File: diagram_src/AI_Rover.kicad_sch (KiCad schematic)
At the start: 11 parts, among them J1 GPIO_PINS, J2 LOGIC_PINS, J3 LOGIC_PINS, J5 POWER_PINS, J6 POWER_PINS, M1 MOTOR_DC_LEFT, M2 MOTOR_DC_RIGHT, SW1 MAIN_POWER_SWITCH

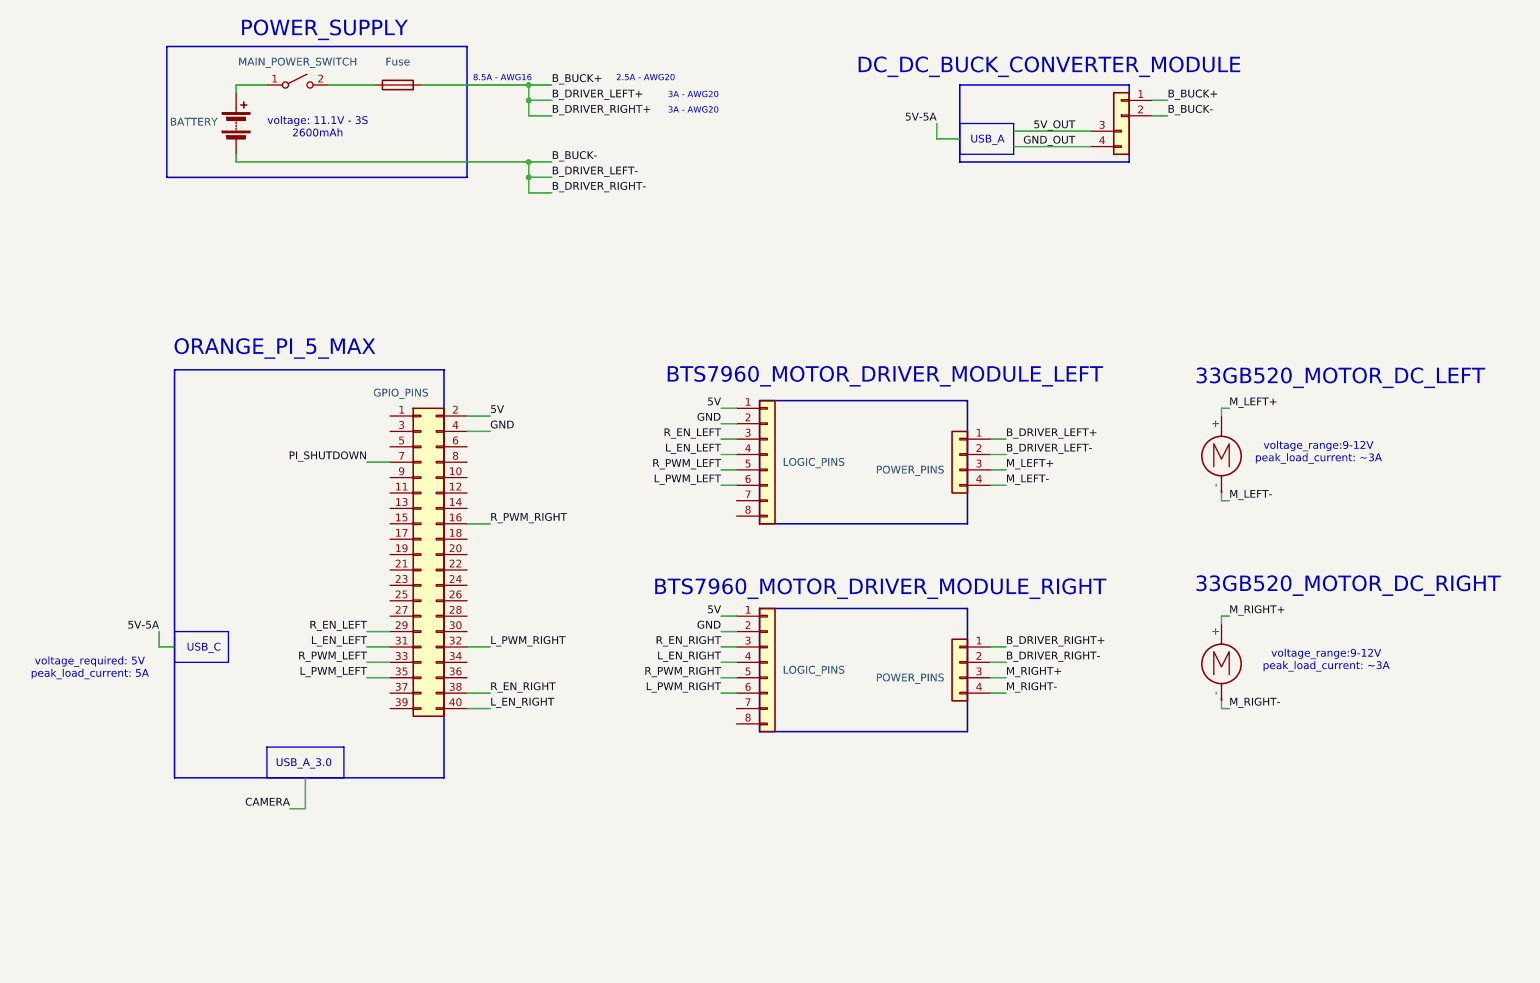
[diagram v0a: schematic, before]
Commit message: Hardware: Add IMU and small improvements to Wiring Schematic
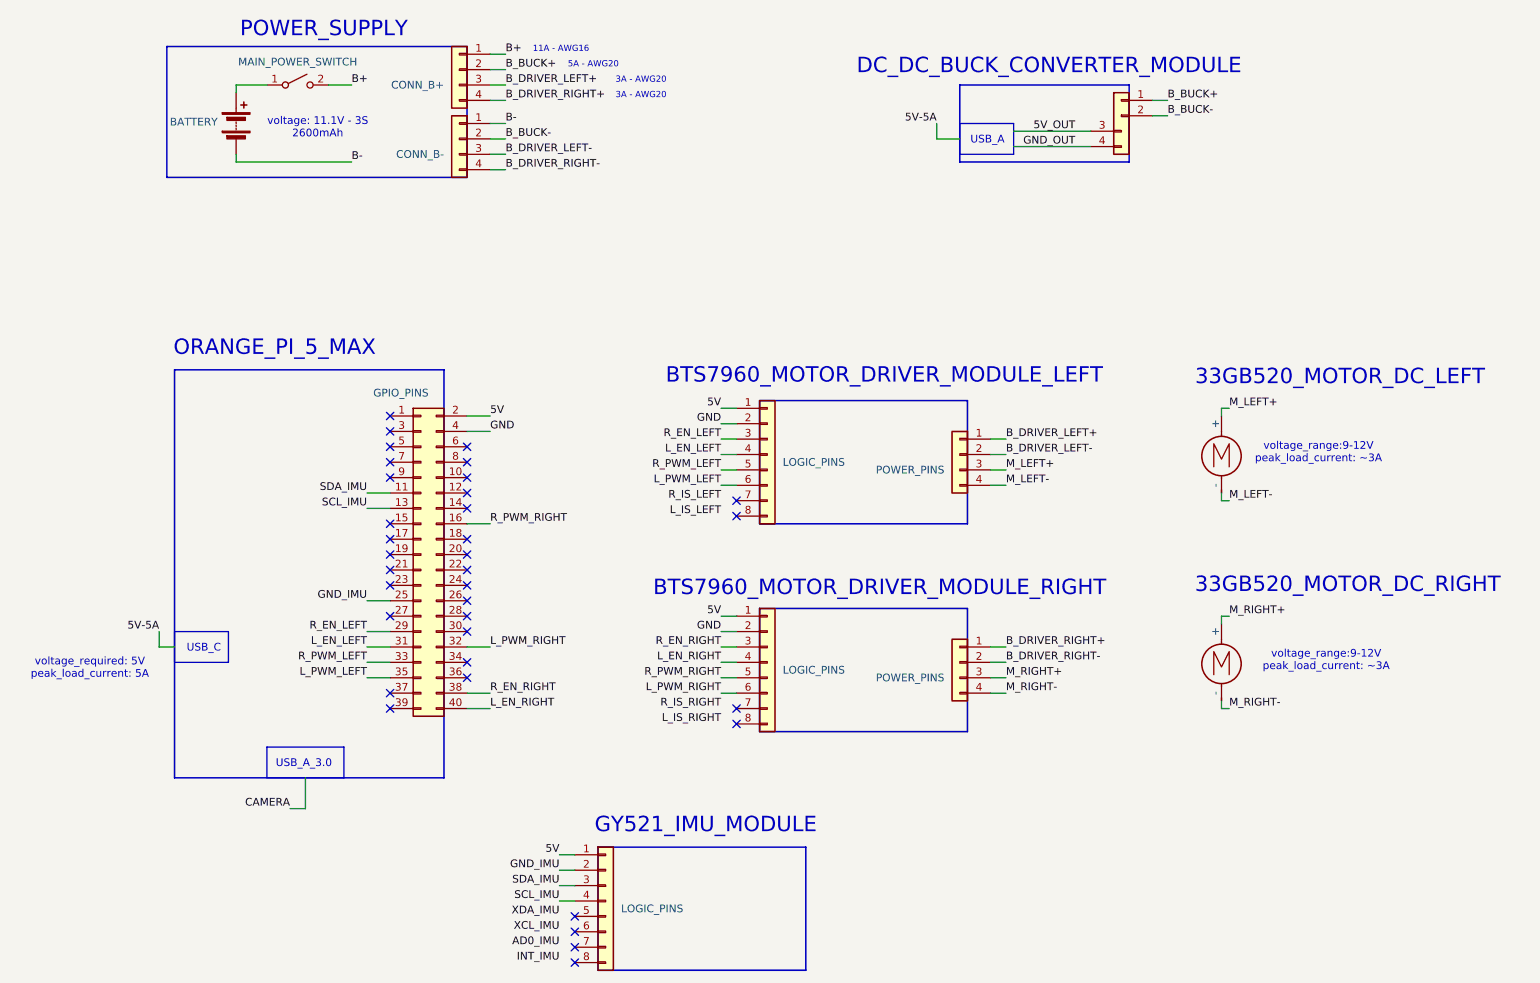
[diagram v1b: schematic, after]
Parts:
- removed F1: Fuse, symbol Device:Fuse
- added J?: CONN_B+, symbol Connector_Generic:Conn_01x04
- added J?: LOGIC_PINS, symbol Connector_Generic:Conn_01x08
- added J?: CONN_B-, symbol Connector_Generic:Conn_01x04
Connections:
- net 5V: now also J?.1 (Pin_1)
- net B_BUCK+: now also J?.2 (Pin_2); no longer J5.1 (Pin_1), J6.1 (Pin_1)
- net B_BUCK-: now also J?.2 (Pin_2); no longer BT1.2 (-), J5.2 (Pin_2), J6.2 (Pin_2)
- net SDA_IMU: now reaches J1.11 (Pin_11)
- net SDA_IMU: now also J?.3 (Pin_3)
- net SCL_IMU: now reaches J1.13 (Pin_13)
- net SCL_IMU: now also J?.4 (Pin_4)
- net GND_IMU: now reaches J1.25 (Pin_25)
- net GND_IMU: now also J?.2 (Pin_2)
- net B+: now reaches SW1.2 (B)
- net B+: now also J?.1 (Pin_1)
- net PI_SHUTDOWN: no longer names the net of J1.7 (Pin_7)
- new net B-: BT1.2 (-), J?.1 (Pin_1)
- new net B_DRIVER_LEFT+: J5.1 (Pin_1), J?.3 (Pin_3)
- new net B_DRIVER_LEFT-: J5.2 (Pin_2), J?.3 (Pin_3)
- new net B_DRIVER_RIGHT+: J6.1 (Pin_1), J?.4 (Pin_4)
- new net B_DRIVER_RIGHT-: J6.2 (Pin_2), J?.4 (Pin_4)
- no-connect marks 0 -> 35
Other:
- note added: "11A - AWG16"
- note added: "5A - AWG20"
- note added: "GY521_IMU_MODULE"
- note removed: "2.5A - AWG20"
- note removed: "8.5A - AWG16"

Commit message: Hardware: Fix wiring issue, cause of GPIO Pins misalignment of 5V pin
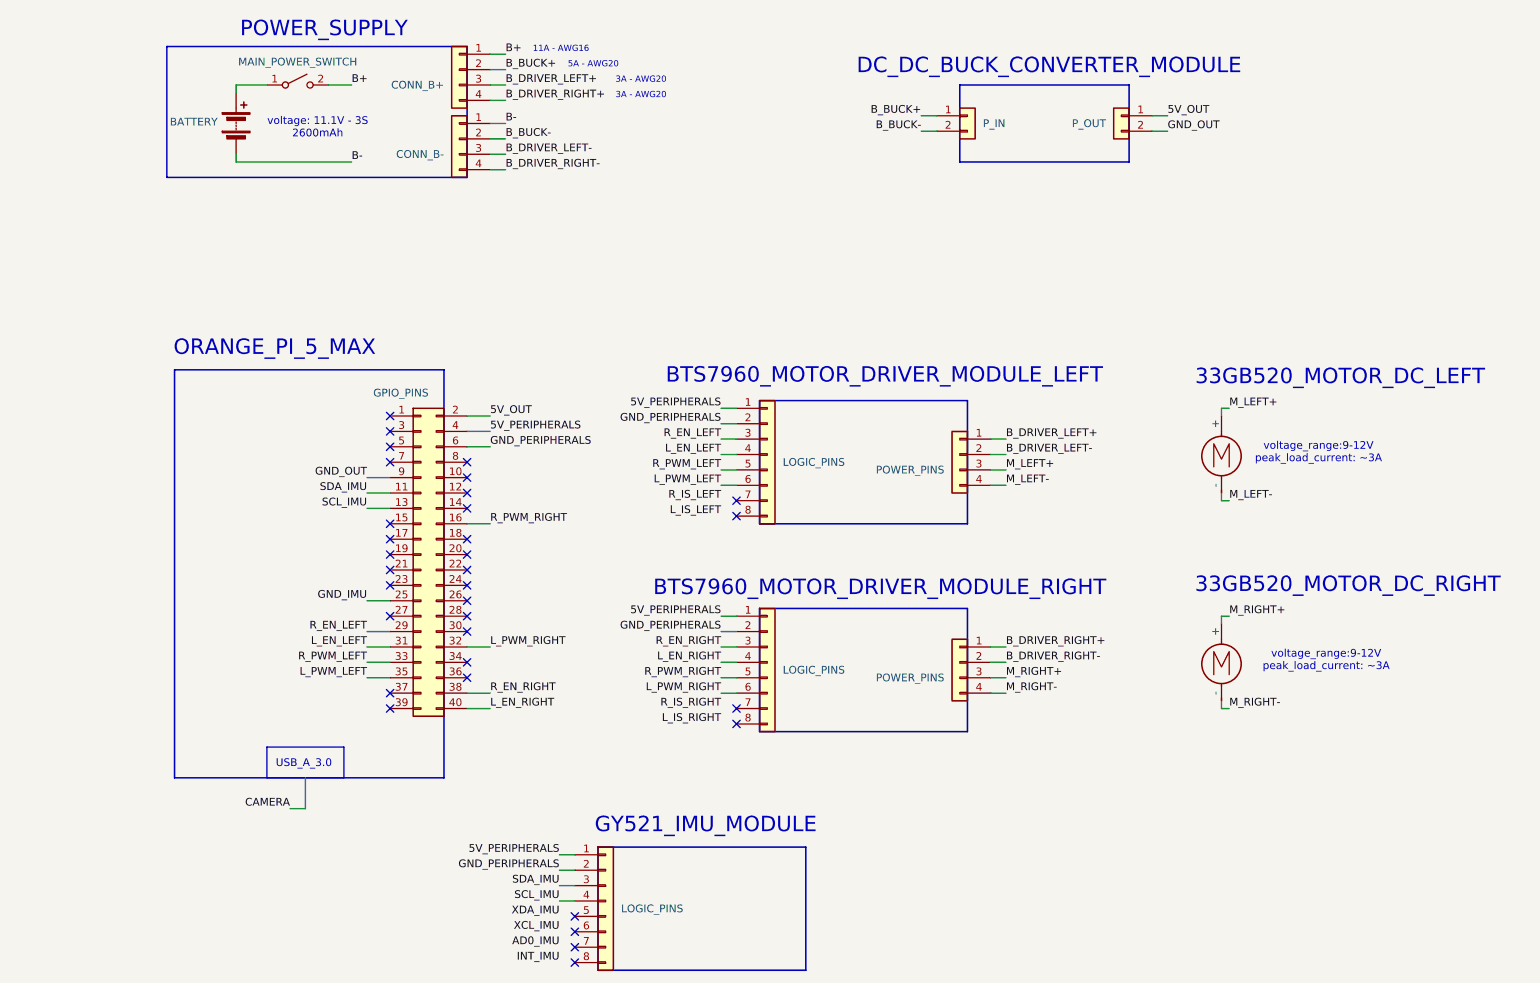
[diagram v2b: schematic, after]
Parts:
- removed J4: (no value), symbol Connector_Generic:Conn_01x04
- added J?: P_OUT, symbol Connector_Generic:Conn_01x02
- added J?: P_IN, symbol Connector_Generic:Conn_01x02
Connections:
- net 5V_OUT: now also J1.2 (Pin_2), J?.1 (Pin_1)
- net B_BUCK+: now also J?.1 (Pin_1)
- net B_BUCK-: now also J?.2 (Pin_2)
- net GND_IMU: no longer J?.2 (Pin_2)
- net GND_OUT: now also J1.9 (Pin_9), J?.2 (Pin_2)
- net GND_PERIPHERALS: now reaches J1.6 (Pin_6)
- net GND_PERIPHERALS: now also J2.2 (Pin_2), J3.2 (Pin_2), J?.2 (Pin_2)
- net 5V renamed 5V_PERIPHERALS
- net 5V_PERIPHERALS: now also J1.4 (Pin_4); no longer J1.2 (Pin_2)
- removed net GND: J1.4 (Pin_4), J2.2 (Pin_2), J3.2 (Pin_2)
- no-connect marks 35 -> 33
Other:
- note removed: "USB_A"
- note removed: "USB_C"
- note removed: "voltage_required: 5V peak_load_current: 5A"

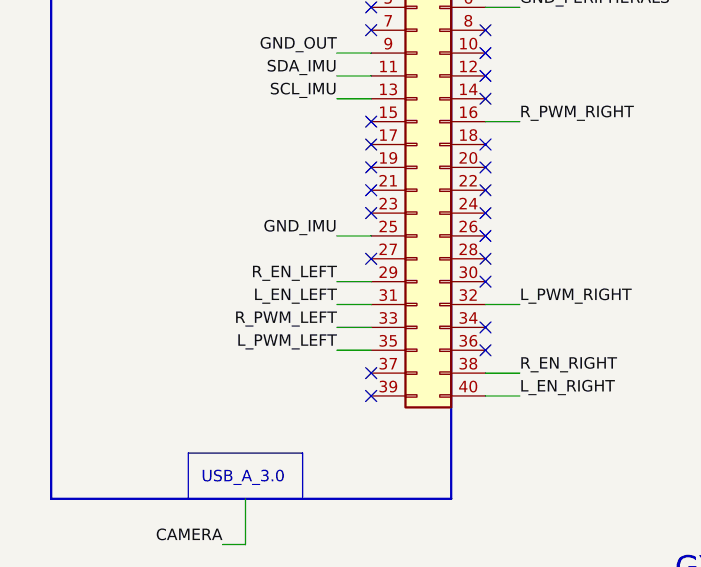
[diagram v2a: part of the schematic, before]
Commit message: Hardware: Fix PWM wiring issue of same PWM line where two different control signals are required
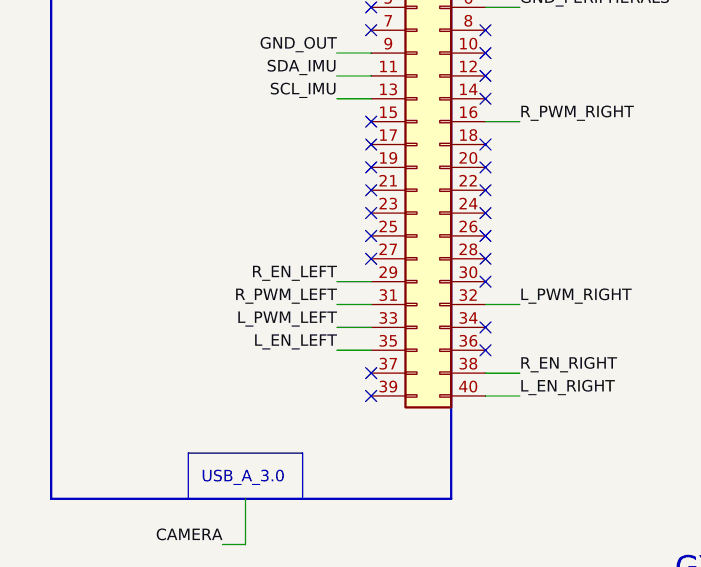
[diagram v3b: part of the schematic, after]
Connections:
- net L_EN_LEFT: now also J1.35 (Pin_35); no longer J1.31 (Pin_31)
- net L_PWM_LEFT: now also J1.33 (Pin_33); no longer J1.35 (Pin_35)
- net R_PWM_LEFT: now also J1.31 (Pin_31); no longer J1.33 (Pin_33)
- net GND_IMU: no longer names the net of J1.25 (Pin_25)
- no-connect marks 33 -> 34
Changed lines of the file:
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@@
+	)
+	(no_connect
+		(at 83.82 120.65)
 	)
 	(no_connect
@@
 	(wire
 		(pts
-			(xy 80.01 120.65) (xy 83.82 120.65)
-		)
-		(stroke
-			(width 0)
-			(type default)
-		)
-	)
-	(wire
-		(pts
 			(xy 222.25 104.14) (xy 220.98 104.14)
 		)
@@
 			(width 0)
 			(type default)
-		)
-	)
-	(label "GND_IMU"
-		(at 80.01 120.65 180)
-		(effects
-			(font
-				(size 1.27 1.27)
-			)
-			(justify right bottom)
 		)
 	)
@@
 		)
 	)
-	(label "R_PWM_LEFT"
+	(label "L_PWM_LEFT"
 		(at 80.01 130.81 180)
 		(effects
@@
 		)
 	)
-	(label "L_PWM_LEFT"
+	(label "L_EN_LEFT"
 		(at 80.01 133.35 180)
 		(effects
@@
 		)
 	)
-	(label "L_EN_LEFT"
+	(label "R_PWM_LEFT"
 		(at 80.01 128.27 180)
 		(effects

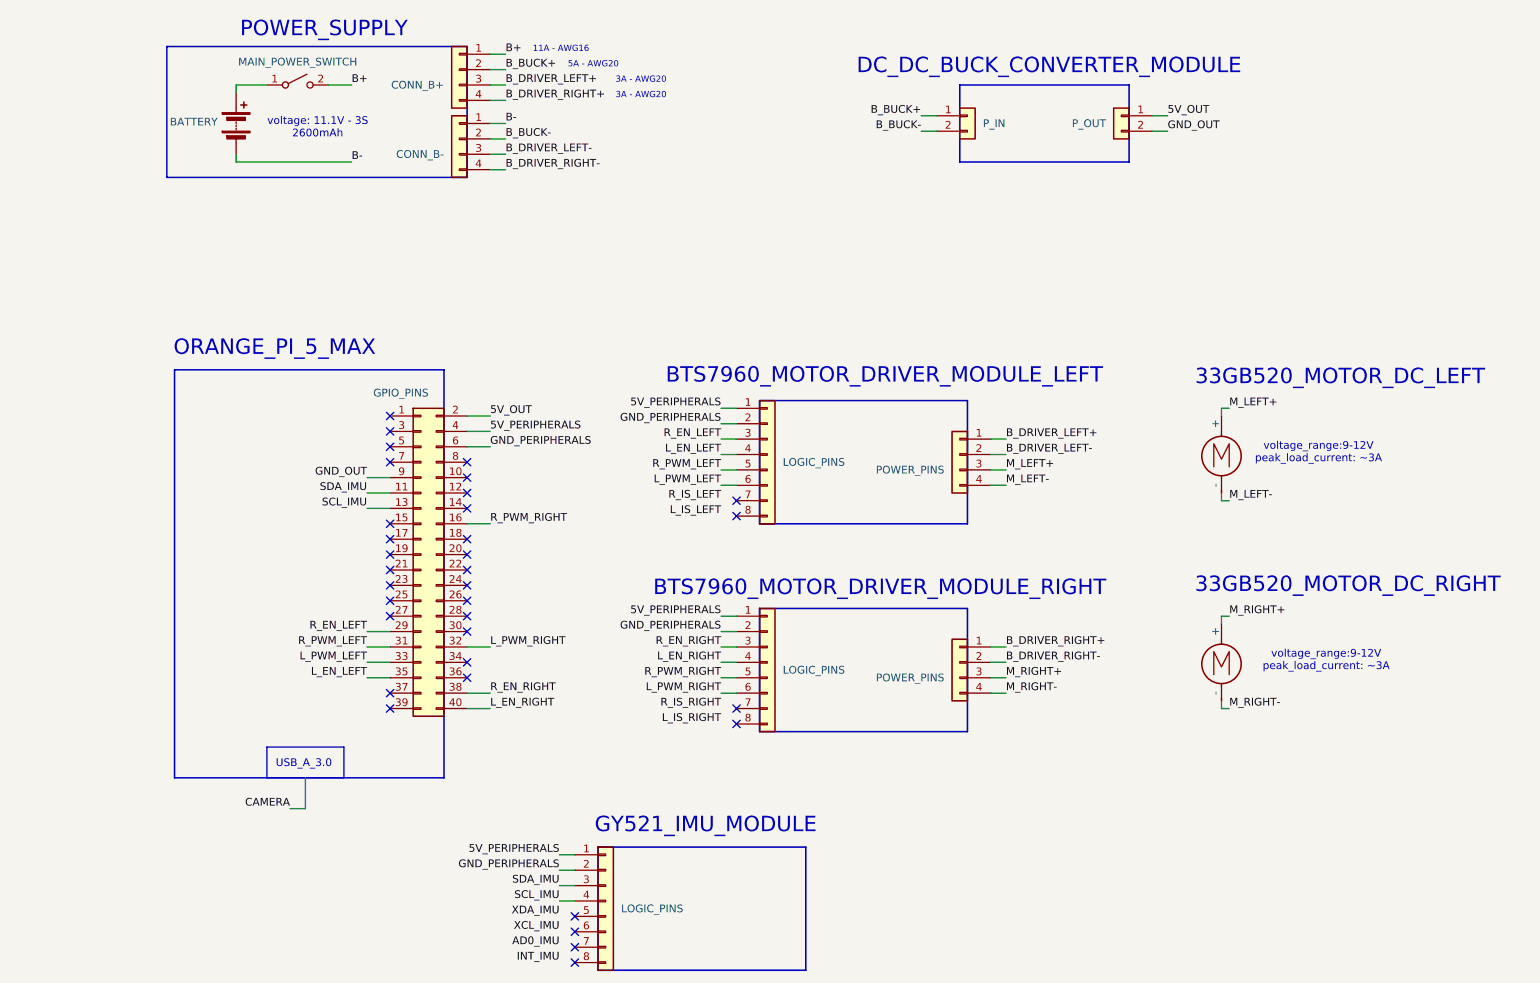
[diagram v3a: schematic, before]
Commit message: Hardware: Change to left-over Rasberry Pi Zero2w since my Orange Pi 5 Max is fried by my stupidity
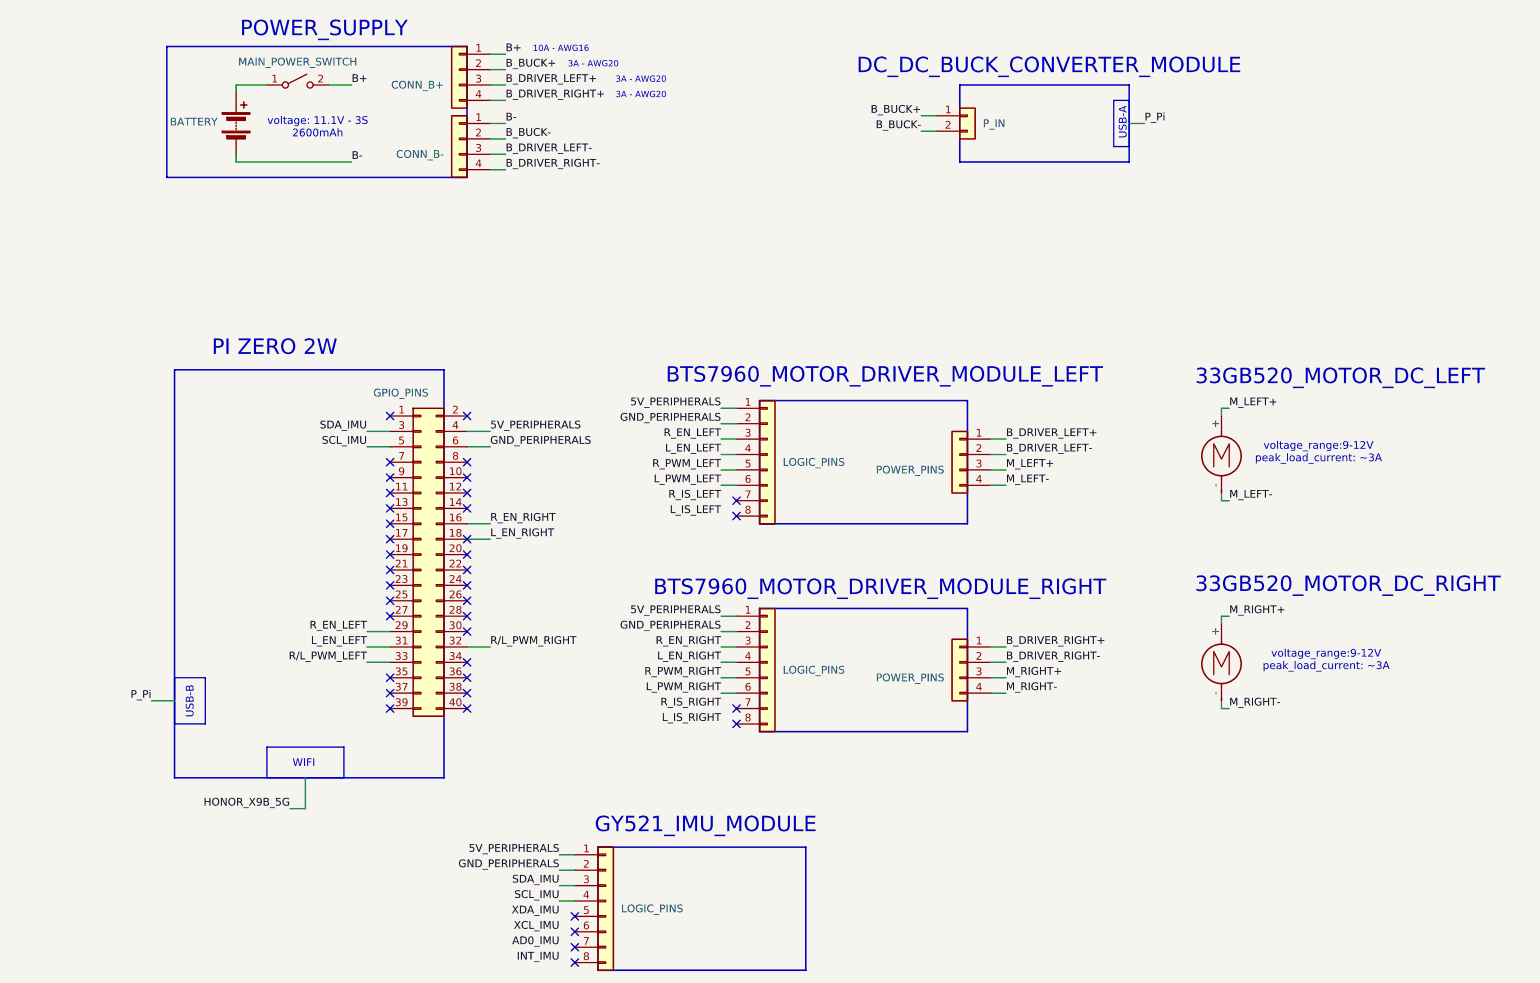
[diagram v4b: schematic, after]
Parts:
- removed J?: P_OUT, symbol Connector_Generic:Conn_01x02
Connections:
- net L_EN_LEFT: now also J1.31 (Pin_31); no longer J1.35 (Pin_35)
- net L_EN_RIGHT: now also J1.18 (Pin_18); no longer J1.40 (Pin_40)
- net L_PWM_LEFT: no longer J1.33 (Pin_33)
- net L_PWM_RIGHT: no longer J1.32 (Pin_32)
- net R_EN_RIGHT: now also J1.16 (Pin_16); no longer J1.38 (Pin_38)
- net R_PWM_LEFT: no longer J1.31 (Pin_31)
- net R_PWM_RIGHT: no longer J1.16 (Pin_16)
- net SCL_IMU: now also J1.5 (Pin_5); no longer J1.13 (Pin_13)
- net SDA_IMU: now also J1.3 (Pin_3); no longer J1.11 (Pin_11)
- net 5V_OUT: no longer names the net of J1.2 (Pin_2)
- net GND_OUT: no longer names the net of J1.9 (Pin_9)
- new net R/L_PWM_LEFT: J1.33 (Pin_33)
- new net R/L_PWM_RIGHT: J1.32 (Pin_32)
- no-connect marks 34 -> 39
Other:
- note added: "10A - AWG16"
- note added: "PI ZERO 2W"
- note added: "USB-A"
- note added: "USB-B"
- note added: "WIFI"
- note removed: "11A - AWG16"
- note removed: "5A - AWG20"
- note removed: "ORANGE_PI_5_MAX"
- note removed: "USB_A_3.0"
